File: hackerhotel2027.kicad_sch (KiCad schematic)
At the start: 22 parts, among them J1 USB device, J2 USB host, U1 CH32V208CBU6_C5713556, U2 TPD4E05U06DQAR, Y1 32.768KHz, Y2 tbd

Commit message: Fill out all component LCSC numbers and fix footprint associations
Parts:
- AE2: LCSC Part (none) -> -
- C1, C2: value 22p -> 9p; LCSC C1555 -> (none); LCSC Part (none) -> C1580
- C3, C4: LCSC Part (none) -> -; now not fitted; now left out of the parts list
- C32, C33, C34, C35: LCSC C307331 -> (none); LCSC Part (none) -> C307331
- C5, C6: LCSC Part (none) -> C327209
- C7: LCSC C5199872 -> (none); LCSC Part (none) -> C5199872
- J1: symbol mch2021-rescue:USB_C_Receptacle_USB2.0-Connector -> Connector:USB_C_Receptacle_USB2.0_16P; LCSC C165948 -> (none); LCSC Part (none) -> C165948
- J2: LCSC C42576 -> (none)
- L1: footprint (none) -> Inductor_SMD:L_01005_0402Metric; LCSC Part (none) -> C703123
- R1, R2: LCSC C25905 -> (none); LCSC Part (none) -> C25905
- R25: LCSC C60490 -> (none); LCSC Part (none) -> C60490
- U2: LCSC C138714 -> (none); LCSC Part (none) -> C138714
- Y1: LCSC C95361 -> (none); LCSC Part (none) -> C95361
- Y2: value tbd -> 32MHz; footprint (none) -> Crystal:Crystal_SMD_3225-4Pin_3.2x2.5mm; LCSC Part (none) -> C9009
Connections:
- net GND: now also J1.SH (SHIELD); no longer J1.S1 (SHIELD)
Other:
- sheet display ports: added BUSY, CS, DC, MOSI, RESETn, SCK; removed none
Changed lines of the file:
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@@
 	(generator_version "10.0")
 	(paper "A4")
+	(title_block
+		(date "2026-06-13")
+	)
 	(junction
 		(at 85.09 102.87)
@@
 			)
 		)
-		(property "LCSC" "C42576"
-			(at 163.83 27.94 0)
-			(hide yes)
-			(show_name no)
-			(do_not_autoplace no)
-			(effects
-				(font
-					(size 1.27 1.27)
-				)
-			)
-		)
 		(pin "5"
 		)
@@
 			)
 		)
-		(property "LCSC" "C138714"
-			(at 231.14 124.46 0)
+		(property "LCSC Part" "C138714"
+			(at 231.14 106.68 0)
 			(hide yes)
 			(show_name no)
@@
 			)
 		)
-		(property "LCSC" "C60490"
+		(property "LCSC Part" "C60490"
 			(at 100.33 78.74 0)
 			(hide yes)
@@
 			)
 		)
-		(property "LCSC" "C25905"
-			(at 245.11 85.09 0)
+		(property "LCSC Part" "C25905"
+			(at 245.11 85.09 90)
 			(hide yes)
 			(show_name no)
@@
 		(body_style 1)
 		(exclude_from_sim no)
-		(in_bom yes)
+		(in_bom no)
 		(on_board yes)
-		(in_pos_files yes)
-		(dnp no)
+		(in_pos_files no)
+		(dnp yes)
 		(property "Reference" "C3"
 			(at 90.678 106.934 0)
@@
 			)
 		)
-		(property "Datasheet" ""
+		(property "Datasheet" "-"
 			(at 90.17 109.22 0)
 			(hide yes)
@@
 			)
 		)
-		(property "LCSC" ""
+		(property "LCSC Part" "-"
 			(at 90.17 109.22 0)
 			(hide yes)
@@
 			)
 		)
-		(property "LCSC" "C5199872"
+		(property "LCSC Part" "C5199872"
 			(at 193.04 80.01 0)
 			(hide yes)
@@
 			)
 		)
-		(property "LCSC" "C307331"
+		(property "LCSC Part" "C307331"
 			(at 62.23 109.22 0)
 			(hide yes)
@@
 			)
 		)
-		(property "LCSC" "C307331"
+		(property "LCSC Part" "C307331"
 			(at 100.33 109.22 0)
 			(hide yes)
@@
 			)
 		)
-		(property "LCSC" "C307331"
+		(property "LCSC Part" "C307331"
 			(at 50.8 109.22 0)
 			(hide yes)
@@
 			)
 		)
-		(property "Datasheet" ""
+		(property "Datasheet" "https://www.lcsc.com/product-detail/C327209.html"
 			(at 193.04 62.23 0)
 			(hide yes)
@@
 			)
 		)
-		(property "LCSC" ""
+		(property "LCSC Part" "C327209"
 			(at 193.04 62.23 0)
 			(hide yes)
@@
 			)
 		)
-		(property "Value" "tbd"
+		(property "Value" "32MHz"
 			(at 88.646 102.616 90)
 			(show_name no)
@@
 			)
 		)
-		(property "Footprint" ""
+		(property "Footprint" "Crystal:Crystal_SMD_3225-4Pin_3.2x2.5mm"
 			(at 92.71 102.87 0)
 			(hide yes)
@@
 			)
 		)
-		(property "Datasheet" ""
+		(property "Datasheet" "https://www.lcsc.com/product-detail/C9009.html"
 			(at 92.71 102.87 0)
 			(hide yes)
@@
 			)
 		)
-		(property "LCSC" ""
+		(property "LCSC Part" "C9009"
 			(at 92.71 102.87 0)
 			(hide yes)
@@
 	)
 	(symbol
-		(lib_id "mch2021-rescue:USB_C_Receptacle_USB2.0-Connector")
+		(lib_id "Connector:USB_C_Receptacle_USB2.0_16P")
 		(at 265.43 92.71 0)
 		(mirror y)
@@
 			)
 		)
-		(property "Datasheet" "https://datasheet.lcsc.com/lcsc/2108131730_Korean-Hroparts-Elec-TYPE-C-31-M-12_C165948.pdf"
+		(property "Datasheet" "https://www.usb.org/sites/default/files/documents/usb_type-c.zip"
 			(at 261.62 92.71 0)
 			(hide yes)
@@
 			)
 		)
-		(property "Description" "TYPE-C-31-M-12"
+		(property "Description" "USB 2.0-only 16P Type-C Receptacle connector"
 			(at 265.43 92.71 0)
 			(hide yes)
@@
 			)
 		)
-		(property "LCSC" "C165948"
+		(property "FT Position Offset" "0,1"
 			(at 265.43 92.71 0)
 			(hide yes)
@@
 			)
 		)
-		(property "FT Position Offset" "0,1"
+		(property "LCSC Part" "C165948"
 			(at 265.43 92.71 0)
 			(hide yes)
@@
 		(pin "B9"
 		)
-		(pin "S1"
+		(pin "SH"
 		)
 		(instances
@@
 			)
 		)
-		(property "Datasheet" ""
+		(property "Datasheet" "-"
 			(at 213.36 48.26 0)
 			(hide yes)
@@
 			)
 		)
+		(property "LCSC Part" "-"
+			(at 213.36 48.26 0)
+			(hide yes)
+			(show_name no)
+			(do_not_autoplace no)
+			(effects
+				(font
+					(size 1.27 1.27)
+				)
+			)
+		)
 		(pin "1"
 		)
@@
 			)
 		)
-		(property "Value" "22p"
+		(property "Value" "9p"
 			(at 80.518 111.506 0)
 			(show_name no)
@@
 			)
 		)
-		(property "Datasheet" "https://datasheet.lcsc.com/lcsc/2304140030_FH--Guangdong-Fenghua-Advanced-Tech-0402CG220J500NT_C1555.pdf"
+		(property "Datasheet" "https://www.lcsc.com/product-detail/C1580.html"
 			(at 80.01 109.22 0)
 			(hide yes)
@@
 			)
 		)
-		(property "LCSC" "C1555"
+		(property "LCSC Part" "C1580"
 			(at 80.01 109.22 0)
 			(hide yes)
@@
 			)
 		)
-		(property "Value" "22p"
+		(property "Value" "9p"
 			(at 85.598 111.76 0)
 			(show_name no)
@@
 			)
 		)
-		(property "Datasheet" "https://datasheet.lcsc.com/lcsc/2304140030_FH--Guangdong-Fenghua-Advanced-Tech-0402CG220J500NT_C1555.pdf"
+		(property "Datasheet" "https://www.lcsc.com/product-detail/C1580.html"
 			(at 85.09 109.22 0)
 			(hide yes)
@@
 			)
 		)
-		(property "LCSC" "C1555"
+		(property "LCSC Part" "C1580"
 			(at 85.09 109.22 0)
 			(hide yes)
@@
 			)
 		)
-		(property "LCSC" "C307331"
+		(property "LCSC Part" "C307331"
 			(at 39.37 109.22 0)
 			(hide yes)
@@
 		(body_style 1)
 		(exclude_from_sim no)
-		(in_bom yes)
+		(in_bom no)
 		(on_board yes)
-		(in_pos_files yes)
-		(dnp no)
+		(in_pos_files no)
+		(dnp yes)
 		(property "Reference" "C4"
 			(at 95.758 106.934 0)
@@
 			)
 		)
-		(property "Datasheet" ""
+		(property "Datasheet" "-"
 			(at 95.25 109.22 0)
 			(hide yes)
@@
 			)
 		)
-		(property "LCSC" ""
+		(property "LCSC Part" "-"
 			(at 95.25 109.22 0)
 			(hide yes)
@@
 			)
 		)
-		(property "Datasheet" ""
+		(property "Datasheet" "https://www.lcsc.com/product-detail/C327209.html"
 			(at 205.74 62.23 0)
 			(hide yes)
@@
 			)
 		)
-		(property "LCSC" ""
+		(property "LCSC Part" "C327209"
 			(at 205.74 62.23 0)
 			(hide yes)
@@
 			)
 		)
-		(property "Footprint" ""
+		(property "Footprint" "Inductor_SMD:L_01005_0402Metric"
 			(at 199.39 55.88 0)
 			(hide yes)
@@
 			)
 		)
-		(property "Datasheet" ""
+		(property "Datasheet" "https://www.lcsc.com/product-detail/C703123.html?s_z=s_p_LQW15AN1N8C00D"
 			(at 199.39 55.88 0)
 			(hide yes)
@@
 			)
 		)
+		(property "LCSC Part" "C703123"
+			(at 199.39 55.88 90)
+			(hide yes)
+			(show_name no)
+			(do_not_autoplace no)
+			(effects
+				(font
+					(size 1.27 1.27)
+				)
+			)
+		)
 		(pin "2"
 		)
@@
 			)
 		)
-		(property "LCSC" "C25905"
-			(at 245.11 82.55 0)
+		(property "LCSC Part" "C25905"
+			(at 245.11 82.55 90)
 			(hide yes)
 			(show_name no)
@@
 			)
 		)
-		(property "LCSC" "C95361"
+		(property "LCSC Part" "C95361"
 			(at 82.55 102.87 0)
 			(hide yes)
@@
 	)
 	(sheet
-		(at 78.74 151.13)
-		(size 20.32 17.78)
+		(at 74.93 144.78)
+		(size 24.13 22.86)
 		(exclude_from_sim no)
 		(in_bom yes)
@@
 		)
 		(property "Sheetname" "display"
-			(at 78.74 150.4184 0)
+			(at 74.93 144.0684 0)
 			(show_name no)
 			(do_not_autoplace no)
@@
 		)
 		(property "Sheetfile" "display.kicad_sch"
-			(at 78.74 169.4946 0)
+			(at 74.93 168.2246 0)
 			(show_name no)
 			(do_not_autoplace no)
@@
 			)
 		)
+		(pin "BUSY" bidirectional
+			(at 74.93 149.86 180)
+			(effects
+				(font
+					(size 1.27 1.27)
+				)
+				(justify left)
+			)
+		)
+		(pin "CS" bidirectional
+			(at 74.93 152.4 180)
+			(effects
+				(font
+					(size 1.27 1.27)
+				)
+				(justify left)
+			)
+		)
+		(pin "DC" bidirectional
+			(at 74.93 154.94 180)
+			(effects
+				(font
+					(size 1.27 1.27)
+				)
+				(justify left)
+			)
+		)
+		(pin "MOSI" bidirectional
+			(at 90.17 144.78 90)
+			(effects
+				(font
+					(size 1.27 1.27)
+				)
+				(justify right)
+			)
+		)
+		(pin "RESETn" bidirectional
+			(at 74.93 160.02 180)
+			(effects
+				(font
+					(size 1.27 1.27)
+				)
+				(justify left)
+			)
+		)
+		(pin "SCK" bidirectional
+			(at 85.09 144.78 90)
+			(effects
+				(font
+					(size 1.27 1.27)
+				)
+				(justify right)
+			)
+		)

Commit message: Small tweaks & initial PCB work
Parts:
- added D1, D10, D11, D12, D13, D14, D15, D2, D4, D6, D7, D9: LED, symbol Device:LED
- added R3, R4, R5, R6: R, symbol Device:R
- added U3: TPD4E05U06DQAR, library:USON-10_L2.5-W1.0-P0.50-BL, symbol TPD4E05U06DQAR:TPD4E05U06DQAR_C138714
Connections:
- net GND: now also U3.3 (GND), U3.8 (GND)
- net SPI_MISO: now also U1.25 (PB14); no longer U1.15 (PA6/ADC6)
- net SPI_MOSI: now also U1.26 (PB15); no longer U1.16 (PA7/ADC7)
- net SPI_SCK: now also U1.24 (PB13); no longer U1.14 (PA5/ADC5)
- net VBUS: now also U3.4 (D2+), U3.5 (D2-), U3.6 (NC), U3.7 (NC)
- net at J2.2 (D-), U1.41 (PB6/USB2DM): now also U3.2 (D1-), U3.9 (NC)
- net at J2.3 (D+), U1.42 (PB7/USB2DP): now also U3.1 (D1+), U3.10 (NC)
- net T2: now reaches U1.11 (PA2/ADC2)
- net T3: now reaches U1.12 (PA3/ADC3)
- net T4: now reaches U1.13 (PA4/ADC4)
- net T8: now reaches U1.17 (PB0/ADC8)
- net T9: now reaches U1.18 (PB1/ADC9)
- net I2C2_SCL: now reaches U1.20 (PB10)
- net I2C2_SDA: now reaches U1.21 (PB11)
- net EPAPER_BUSY: now reaches U1.23 (PB12)
- net SPI_CS_EPAPER: now reaches U1.27 (PA8)
- net SPI_CS_FLASH: now reaches U1.28 (PA9)
- net EPAPER_DC: now reaches U1.29 (PA10)
- net LM4: now reaches U1.37 (PA15)
- net LM4: now also R6.1
- net LM3: now reaches U1.38 (PB3)
- net LM3: now also R5.1
- net LM2: now reaches U1.39 (PB4)
- net LM2: now also R4.1
- net LM1: now reaches U1.40 (PB5)
- net LM1: now also R3.1
- net BOOT: now reaches U1.43 (BOOT0)
- net I2C1_SCL: now reaches U1.44 (PB8)
- net I2C1_SDA: now reaches U1.45 (PB9)
- net BTN1 renamed PWR_BTN
- net BTN2 renamed T1
- new net: D12.1 (K), D13.2 (A), D14.1 (K), D15.2 (A), D7.1 (K), D9.2 (A), R6.2
- new net: D1.1 (K), D12.2 (A), D13.1 (K), D2.2 (A), D4.2 (A), D6.1 (K), R4.2
- new net: D6.2 (A), D7.2 (A)
- new net: D10.1 (K), D11.2 (A), D4.1 (K), D9.1 (K), R5.2
- new net: D1.2 (A), D10.2 (A), D11.1 (K), D14.2 (A), D15.1 (K), D2.1 (K), R3.2
- new net T5: U1.14 (PA5/ADC5)
- new net T6: U1.15 (PA6/ADC6)
- new net T7: U1.16 (PA7/ADC7)
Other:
- moved on the sheet: J2

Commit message: Switch to WCH ledmatrix controller, add loads of LEDs
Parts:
- removed AE2: Antenna, RF_Antenna:Texas_SWRA117D_2.4GHz_Right, symbol Device:Antenna_Loop
- removed C1, C2: 9p, Capacitor_SMD:C_0402_1005Metric, symbol Device:C
- removed C3, C4: (no value), Capacitor_SMD:C_0402_1005Metric, symbol Device:C
- removed C32: 100n, Capacitor_SMD:C_0402_1005Metric, symbol symbols:C
- removed C5, C6: 1.8p, Capacitor_SMD:C_0402_1005Metric, symbol Device:C
- removed C7: 1u, Capacitor_SMD:C_0603_1608Metric, symbol mch2021-rescue:C-Device
- removed J2: USB host, library:USB-A-TH_JTJ-USB-A-F-10.0-010, symbol Connector:USB_A
- removed L1: 1.8n, Inductor_SMD:L_01005_0402Metric, symbol Device:L
- removed R25: 10k, Resistor_SMD:R_0402_1005Metric, symbol symbols:R
- removed U1: CH32V208CBU6_C5713556, ch32v208:QFN-48_L5.0-W5.0-P0.35-BL-EP-A, symbol ch32v208:CH32V208CBU6_C5713556
- removed U3: TPD4E05U06DQAR, library:USON-10_L2.5-W1.0-P0.50-BL, symbol TPD4E05U06DQAR:TPD4E05U06DQAR_C138714
- removed Y1: 32.768KHz, Crystal:Crystal_SMD_3215-2Pin_3.2x1.5mm, symbol symbols:Crystal_Small
- removed Y2: 32MHz, Crystal:Crystal_SMD_3225-4Pin_3.2x2.5mm, symbol symbols:Crystal_Small
- added D100, D101, D102, D103, D104, D105, D106, D107, D108, D109, D110, D111, D112, D113, D114, D115, D116, D117, D118, D119, D120, D121, D122, D123, D124, D125, D126, D127, D128, D129, D130, D131, D132, D133, D134, D135, D136, D137, D138, D139, D140, D141, D142, D143, D144, D145, D146, D147, D148, D149, D150, D158, D159, D16, D160, D161, D162, D163, D164, D165, D166, D167, D168, D169, D17, D170, D171, D172, D173, D174, D175, D176, D177, D178, D179, D18, D180, D181, D182, D183, D184, D185, D186, D187, D188, D189, D19, D190, D191, D192, D193, D194, D195, D196, D197, D198, D199, D20, D200, D201, D202, D203, D204, D205, D206, D207, D208, D21, D216, D217, D218, D219, D22, D220, D221, D222, D223, D224, D225, D226, D227, D228, D229, D23, D230, D231, D232, D233, D234, D235, D236, D237, D238, D239, D24, D240, D241, D242, D243, D244, D245, D246, D247, D248, D249, D25, D250, D251, D252, D253, D254, D255, D256, D257, D258, D259, D26, D260, D261, D262, D263, D264, D265, D266, D27, D274, D275, D276, D277, D278, D279, D28, D280, D281, D282, D283, D284, D285, D286, D287, D288, D289, D29, D290, D291, D292, D293, D294, D295, D296, D297, D298, D299, D3, D30, D300, D301, D302, D303, D304, D305, D306, D307, D308, D309, D31, D310, D311, D312, D313, D314, D32, D33, D34, D42, D43, D44, D45, D46, D47, D48, D49, D5, D50, D51, D52, D53, D54, D55, D56, D57, D58, D59, D60, D61, D62, D63, D64, D65, D66, D67, D68, D69, D70, D71, D72, D73, D74, D75, D76, D77, D78, D79, D8, D80, D81, D82, D83, D84, D85, D86, D87, D88, D89, D90, D91, D92: LED, LED_SMD:LED_0402_1005Metric, symbol Device:LED
- added D151, D152, D153, D154, D155, D156, D157, D209, D210, D211, D212, D213, D214, D215, D267, D268, D269, D270, D271, D272, D273, D35, D36, D37, D38, D39, D40, D41, D93, D94, D95, D96, D97, D98, D99: NH-B1515RGBA-GF, led:LED-SMD-4P-L1.6-W1.5_NH-B1515RGBA-GF, symbol led:NH-B1515RGBA-GF
- added R1, R10, R11, R12, R13, R14, R15, R16, R17, R18, R19, R2, R20, R21, R22, R23, R24, R7, R8, R9: R, Resistor_SMD:R_0402_1005Metric, symbol Device:R
- added U1: CH643Q, ch643:LQFP-64_L7.0-W7.0-P0.40-LS9.2-BL, symbol ch643:CH643Q
- D1, D10, D11, D12, D13, D14, D15, D2, D4, D6, D7, D9: footprint (none) -> LED_SMD:LED_0402_1005Metric; LCSC Part (none) -> C779450
- R3, R4, R5, R6: footprint (none) -> Resistor_SMD:R_0402_1005Metric
- renumbered C35 to C1, C34 to C2, C33 to C3, R1 to R25, R2 to R26
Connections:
- net CC1: now also U1.55 (PC14/CC1/T1C3_/T2C2_)
- net CC2: now also U1.56 (PC15/CC2/T2C3_/T1ET_)
- net GND: now also U1.1 (GND), U1.30 (GND30)
- net T1: now also U1.9 (PC0/TX2_/T2C4_)
- net T2: now also U1.10 (PC1/T1C2_/T2C1N_)
- net T3: now also U1.11 (PC2/T1C3_/T2C2N_)
- net T4: now also U1.12 (PC3/RTS2_/T1C4_)
- net R6b: now reaches D6.2 (A)
- net R6b: now also R6.2, D105.2 (A), D122.2 (A), D139.2 (A), D163.2 (A), D180.2 (A), D197.2 (A), D221.2 (A), D23.2 (A), D238.2 (A), D255.2 (A), D279.2 (A), D296.2 (A), D47.2 (A), D64.2 (A), D81.2 (A); no longer D7.2 (A)
- net C1: now reaches D10.1 (K), D4.1 (K), D9.1 (K)
- net C1: now also D1.1 (K), D11.1 (K), D12.1 (K), D13.1 (K), D14.1 (K), D15.1 (K), D2.1 (K), D6.1 (K), D7.1 (K), D16.1 (K), D17.1 (K), D3.1 (K), D35.1 (RED), D36.1 (RED), D37.1 (RED), D38.1 (RED), D39.1 (RED), D40.1 (RED), D41.1 (RED), D5.1 (K), D8.1 (K), U1.25 (PB0/TX4/T1C2N_/O1P0); no longer D11.2 (A), R5.2
- net USB_DN: now reaches J1.A7 (D-), J1.B7 (D-), U2.1 (D1+), U2.10 (NC)
- net USB_DN: now also U1.43 (PC16/UDM/T1C4/TX4_)
- net USB_DP: now reaches J1.A6 (D+), J1.B6 (D+), U2.2 (D1-), U2.9 (NC)
- net USB_DP: now also U1.44 (PC17/UDP/RTS1/TX4_)
- net LM1 renamed R3
- net R3: now also U1.17 (PA2/TX2/T2C3/O2O1)
- net LM2 renamed R4
- net R4: now also U1.18 (PA3/T2C4/O1O0)
- net LM3 renamed R5
- net R5: now also U1.21 (PA4/CS/O2O0/RTS3_)
- net LM4 renamed R6
- net R6: now also U1.22 (PA5/SCK/TX4_/CTS4_)
- new net: D152.2, D210.2, D268.2, D309.2 (A), D36.2, D94.2, R19.2
- new net: D151.2, D209.2, D267.2, D308.2 (A), D35.2, D93.2, R18.2
- new net: D156.2, D214.2, D272.2, D313.2 (A), D40.2, D98.2, R23.2
- new net: D116.2 (A), D133.2 (A), D150.2 (A), D17.2 (A), D174.2 (A), D191.2 (A), D208.2 (A), D232.2 (A), D249.2 (A), D266.2 (A), D290.2 (A), D307.2 (A), D34.2 (A), D58.2 (A), D75.2 (A), D92.2 (A), R17.2
- new net: D114.2 (A), D131.2 (A), D148.2 (A), D15.2 (A), D172.2 (A), D189.2 (A), D206.2 (A), D230.2 (A), D247.2 (A), D264.2 (A), D288.2 (A), D305.2 (A), D32.2 (A), D56.2 (A), D73.2 (A), D90.2 (A), R15.2
- new net: D153.2, D211.2, D269.2, D310.2 (A), D37.2, D95.2, R20.2
- new net: D157.2, D215.2, D273.2, D314.2 (A), D41.2, D99.2, R24.2
- new net: D115.2 (A), D132.2 (A), D149.2 (A), D16.2 (A), D173.2 (A), D190.2 (A), D207.2 (A), D231.2 (A), D248.2 (A), D265.2 (A), D289.2 (A), D306.2 (A), D33.2 (A), D57.2 (A), D74.2 (A), D91.2 (A), R16.2
- new net: D154.2, D212.2, D270.2, D311.2 (A), D38.2, D96.2, R21.2
- new net: D155.2, D213.2, D271.2, D312.2 (A), D39.2, D97.2, R22.2
- new net C10: D175.1 (K), D176.1 (K), D177.1 (K), D178.1 (K), D179.1 (K), D180.1 (K), D181.1 (K), D182.1 (K), D183.1 (K), D184.1 (K), D185.1 (K), D186.1 (K), D187.1 (K), D188.1 (K), D189.1 (K), D190.1 (K), D191.1 (K), D209.1 (RED), D210.1 (RED), D211.1 (RED), D212.1 (RED), D213.1 (RED), D214.1 (RED), D215.1 (RED), U1.40 (PB9/T1C1/MCO/TX4_40)
- new net C11: D192.1 (K), D193.1 (K), D194.1 (K), D195.1 (K), D196.1 (K), D197.1 (K), D198.1 (K), D199.1 (K), D200.1 (K), D201.1 (K), D202.1 (K), D203.1 (K), D204.1 (K), D205.1 (K), D206.1 (K), D207.1 (K), D208.1 (K), D209.4 (GREEN), D210.4 (GREEN), D211.4 (GREEN), D212.4 (GREEN), D213.4 (GREEN), D214.4 (GREEN), D215.4 (GREEN), U1.41 (PB10/TX1/T1C241)
- new net C12: D209.3 (BLUE), D210.3 (BLUE), D211.3 (BLUE), D212.3 (BLUE), D213.3 (BLUE), D214.3 (BLUE), D215.3 (BLUE), D216.1 (K), D217.1 (K), D218.1 (K), D219.1 (K), D220.1 (K), D221.1 (K), D222.1 (K), D223.1 (K), D224.1 (K), D225.1 (K), D226.1 (K), D227.1 (K), D228.1 (K), D229.1 (K), D230.1 (K), D231.1 (K), D232.1 (K), U1.42 (PB11/T1C3/T2C1N_/RX142)
- new net C13: D233.1 (K), D234.1 (K), D235.1 (K), D236.1 (K), D237.1 (K), D238.1 (K), D239.1 (K), D240.1 (K), D241.1 (K), D242.1 (K), D243.1 (K), D244.1 (K), D245.1 (K), D246.1 (K), D247.1 (K), D248.1 (K), D249.1 (K), D267.1 (RED), D268.1 (RED), D269.1 (RED), D270.1 (RED), D271.1 (RED), D272.1 (RED), D273.1 (RED), U1.46 (PB12/T1C4_/T2C2N_46)
- new net C14: D250.1 (K), D251.1 (K), D252.1 (K), D253.1 (K), D254.1 (K), D255.1 (K), D256.1 (K), D257.1 (K), D258.1 (K), D259.1 (K), D260.1 (K), D261.1 (K), D262.1 (K), D263.1 (K), D264.1 (K), D265.1 (K), D266.1 (K), D267.4 (GREEN), D268.4 (GREEN), D269.4 (GREEN), D270.4 (GREEN), D271.4 (GREEN), D272.4 (GREEN), D273.4 (GREEN), U1.48 (PB13/TX4_48)
- new net C15: D267.3 (BLUE), D268.3 (BLUE), D269.3 (BLUE), D270.3 (BLUE), D271.3 (BLUE), D272.3 (BLUE), D273.3 (BLUE), D274.1 (K), D275.1 (K), D276.1 (K), D277.1 (K), D278.1 (K), D279.1 (K), D280.1 (K), D281.1 (K), D282.1 (K), D283.1 (K), D284.1 (K), D285.1 (K), D286.1 (K), D287.1 (K), D288.1 (K), D289.1 (K), D290.1 (K), U1.49 (PB14/RX3_)
- new net C16: D291.1 (K), D292.1 (K), D293.1 (K), D294.1 (K), D295.1 (K), D296.1 (K), D297.1 (K), D298.1 (K), D299.1 (K), D300.1 (K), D301.1 (K), D302.1 (K), D303.1 (K), D304.1 (K), D305.1 (K), D306.1 (K), D307.1 (K), D308.1 (K), D309.1 (K), D310.1 (K), D311.1 (K), D312.1 (K), D313.1 (K), D314.1 (K), U1.54 (PB15/T2C2_/SCK_/CTS4)
- new net C2: D18.1 (K), D19.1 (K), D20.1 (K), D21.1 (K), D22.1 (K), D23.1 (K), D24.1 (K), D25.1 (K), D26.1 (K), D27.1 (K), D28.1 (K), D29.1 (K), D30.1 (K), D31.1 (K), D32.1 (K), D33.1 (K), D34.1 (K), D35.4 (GREEN), D36.4 (GREEN), D37.4 (GREEN), D38.4 (GREEN), D39.4 (GREEN), D40.4 (GREEN), D41.4 (GREEN), U1.26 (PB1/T1C3N_/RX4)
- new net C3: D35.3 (BLUE), D36.3 (BLUE), D37.3 (BLUE), D38.3 (BLUE), D39.3 (BLUE), D40.3 (BLUE), D41.3 (BLUE), D42.1 (K), D43.1 (K), D44.1 (K), D45.1 (K), D46.1 (K), D47.1 (K), D48.1 (K), D49.1 (K), D50.1 (K), D51.1 (K), D52.1 (K), D53.1 (K), D54.1 (K), D55.1 (K), D56.1 (K), D57.1 (K), D58.1 (K), U1.27 (PB2/C2O/RX1_27)
- new net C4: D59.1 (K), D60.1 (K), D61.1 (K), D62.1 (K), D63.1 (K), D64.1 (K), D65.1 (K), D66.1 (K), D67.1 (K), D68.1 (K), D69.1 (K), D70.1 (K), D71.1 (K), D72.1 (K), D73.1 (K), D74.1 (K), D75.1 (K), D93.1 (RED), D94.1 (RED), D95.1 (RED), D96.1 (RED), D97.1 (RED), D98.1 (RED), D99.1 (RED), U1.28 (PB3/TX3/C3O/T2C3_)
- new net C5: D76.1 (K), D77.1 (K), D78.1 (K), D79.1 (K), D80.1 (K), D81.1 (K), D82.1 (K), D83.1 (K), D84.1 (K), D85.1 (K), D86.1 (K), D87.1 (K), D88.1 (K), D89.1 (K), D90.1 (K), D91.1 (K), D92.1 (K), D93.4 (GREEN), D94.4 (GREEN), D95.4 (GREEN), D96.4 (GREEN), D97.4 (GREEN), D98.4 (GREEN), D99.4 (GREEN), U1.29 (PB4/T2C4_/T3C1_/T2BK_)
- new net C6: D100.1 (K), D101.1 (K), D102.1 (K), D103.1 (K), D104.1 (K), D105.1 (K), D106.1 (K), D107.1 (K), D108.1 (K), D109.1 (K), D110.1 (K), D111.1 (K), D112.1 (K), D113.1 (K), D114.1 (K), D115.1 (K), D116.1 (K), D93.3 (BLUE), D94.3 (BLUE), D95.3 (BLUE), D96.3 (BLUE), D97.3 (BLUE), D98.3 (BLUE), D99.3 (BLUE), U1.32 (PB5/O1O1/T3C2_)
- new net C7: D117.1 (K), D118.1 (K), D119.1 (K), D120.1 (K), D121.1 (K), D122.1 (K), D123.1 (K), D124.1 (K), D125.1 (K), D126.1 (K), D127.1 (K), D128.1 (K), D129.1 (K), D130.1 (K), D131.1 (K), D132.1 (K), D133.1 (K), D151.1 (RED), D152.1 (RED), D153.1 (RED), D154.1 (RED), D155.1 (RED), D156.1 (RED), D157.1 (RED), U1.33 (PB6/T1C1N/CTS3/O1N133)
- new net C8: D134.1 (K), D135.1 (K), D136.1 (K), D137.1 (K), D138.1 (K), D139.1 (K), D140.1 (K), D141.1 (K), D142.1 (K), D143.1 (K), D144.1 (K), D145.1 (K), D146.1 (K), D147.1 (K), D148.1 (K), D149.1 (K), D150.1 (K), D151.4 (GREEN), D152.4 (GREEN), D153.4 (GREEN), D154.4 (GREEN), D155.4 (GREEN), D156.4 (GREEN), D157.4 (GREEN), U1.34 (PB7/T1C2N/RTS3_/O2P234)
- new net C9: D151.3 (BLUE), D152.3 (BLUE), D153.3 (BLUE), D154.3 (BLUE), D155.3 (BLUE), D156.3 (BLUE), D157.3 (BLUE), D158.1 (K), D159.1 (K), D160.1 (K), D161.1 (K), D162.1 (K), D163.1 (K), D164.1 (K), D165.1 (K), D166.1 (K), D167.1 (K), D168.1 (K), D169.1 (K), D170.1 (K), D171.1 (K), D172.1 (K), D173.1 (K), D174.1 (K), U1.35 (PB8/T1C3N/O1P135)
- new net R1: R1.1, U1.15 (PA0/T2C1/CTS2)
- new net R10: R10.1, U1.58 (PA9/MOSI_/MISO_/RX4_)
- new net R10b: D10.2 (A), D109.2 (A), D126.2 (A), D143.2 (A), D167.2 (A), D184.2 (A), D201.2 (A), D225.2 (A), D242.2 (A), D259.2 (A), D27.2 (A), D283.2 (A), D300.2 (A), D51.2 (A), D68.2 (A), D85.2 (A), R10.2
- new net R11: R11.1, U1.59 (PA10/SCL/TX1_/MOSI_)
- new net R11b: D11.2 (A), D110.2 (A), D127.2 (A), D144.2 (A), D168.2 (A), D185.2 (A), D202.2 (A), D226.2 (A), D243.2 (A), D260.2 (A), D28.2 (A), D284.2 (A), D301.2 (A), D52.2 (A), D69.2 (A), D86.2 (A), R11.2
- new net R12: R12.1, U1.60 (PA11/SDA/SCK_/RX1_)
- new net R12b: D111.2 (A), D12.2 (A), D128.2 (A), D145.2 (A), D169.2 (A), D186.2 (A), D203.2 (A), D227.2 (A), D244.2 (A), D261.2 (A), D285.2 (A), D29.2 (A), D302.2 (A), D53.2 (A), D70.2 (A), D87.2 (A), R12.2
- new net R13: R13.1, U1.61 (PA12/CS_/T2C2_/T2C1N_)
- new net R13b: D112.2 (A), D129.2 (A), D13.2 (A), D146.2 (A), D170.2 (A), D187.2 (A), D204.2 (A), D228.2 (A), D245.2 (A), D262.2 (A), D286.2 (A), D30.2 (A), D303.2 (A), D54.2 (A), D71.2 (A), D88.2 (A), R13.2
- new net R14: R14.1, U1.62 (PA13/SCL_/RTS4_)
- new net R14b: D113.2 (A), D130.2 (A), D14.2 (A), D147.2 (A), D171.2 (A), D188.2 (A), D205.2 (A), D229.2 (A), D246.2 (A), D263.2 (A), D287.2 (A), D304.2 (A), D31.2 (A), D55.2 (A), D72.2 (A), D89.2 (A), R14.2
- new net R15: R15.1, U1.63 (PA14/SDA_/RTS1_)
- new net R16: R16.1, U1.2 (PA15/TX2_)
- new net R17: R17.1, U1.3 (PA16/RX2_)
- new net R18: R18.1, U1.4 (PA17/CTS2_)
- new net R19: R19.1, U1.5 (PA18/TX3_/T2ET_)
- new net R1b: D1.2 (A), D100.2 (A), D117.2 (A), D134.2 (A), D158.2 (A), D175.2 (A), D18.2 (A), D192.2 (A), D216.2 (A), D233.2 (A), D250.2 (A), D274.2 (A), D291.2 (A), D42.2 (A), D59.2 (A), D76.2 (A), R1.2
- new net R2: R2.1, U1.16 (PA1/RTS2/T2C2)
- new net R20: R20.1, U1.6 (PA19/T2ET/RX2_)
- new net R21: R21.1, U1.7 (PA20/TX2_/T2BK)
- new net R22: R22.1, U1.8 (PA21/T2C1N/RTS2_)
- new net R23: R23.1, U1.13 (PA22/T2C2N/C2N0)
- new net R24: R24.1, U1.14 (PA23/T2C3N/C1N1)
- new net R2b: D101.2 (A), D118.2 (A), D135.2 (A), D159.2 (A), D176.2 (A), D19.2 (A), D193.2 (A), D2.2 (A), D217.2 (A), D234.2 (A), D251.2 (A), D275.2 (A), D292.2 (A), D43.2 (A), D60.2 (A), D77.2 (A), R2.2
- new net R3b: D102.2 (A), D119.2 (A), D136.2 (A), D160.2 (A), D177.2 (A), D194.2 (A), D20.2 (A), D218.2 (A), D235.2 (A), D252.2 (A), D276.2 (A), D293.2 (A), D3.2 (A), D44.2 (A), D61.2 (A), D78.2 (A), R3.2
- new net R4b: D103.2 (A), D120.2 (A), D137.2 (A), D161.2 (A), D178.2 (A), D195.2 (A), D21.2 (A), D219.2 (A), D236.2 (A), D253.2 (A), D277.2 (A), D294.2 (A), D4.2 (A), D45.2 (A), D62.2 (A), D79.2 (A), R4.2
- new net R5b: D104.2 (A), D121.2 (A), D138.2 (A), D162.2 (A), D179.2 (A), D196.2 (A), D22.2 (A), D220.2 (A), D237.2 (A), D254.2 (A), D278.2 (A), D295.2 (A), D46.2 (A), D5.2 (A), D63.2 (A), D80.2 (A), R5.2
- new net R7: R7.1, U1.23 (PA6/MISO/T3C1/RTS4_)
- new net R7b: D106.2 (A), D123.2 (A), D140.2 (A), D164.2 (A), D181.2 (A), D198.2 (A), D222.2 (A), D239.2 (A), D24.2 (A), D256.2 (A), D280.2 (A), D297.2 (A), D48.2 (A), D65.2 (A), D7.2 (A), D82.2 (A), R7.2
- new net R8: R8.1, U1.24 (PA7/MOSI/T3C2/T1C1N_)
- new net R8b: D107.2 (A), D124.2 (A), D141.2 (A), D165.2 (A), D182.2 (A), D199.2 (A), D223.2 (A), D240.2 (A), D25.2 (A), D257.2 (A), D281.2 (A), D298.2 (A), D49.2 (A), D66.2 (A), D8.2 (A), D83.2 (A), R8.2
- new net R9: R9.1, U1.57 (PA8/MISO_/RTS4/RTS1_)
- new net R9b: D108.2 (A), D125.2 (A), D142.2 (A), D166.2 (A), D183.2 (A), D200.2 (A), D224.2 (A), D241.2 (A), D258.2 (A), D26.2 (A), D282.2 (A), D299.2 (A), D50.2 (A), D67.2 (A), D84.2 (A), D9.2 (A), R9.2
- new net SWCK: U1.47 (PC19/DCK/T2C1_)
- new net SWIO: U1.45 (PC18/DIO/TX3_/T2C1N_)
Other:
- removed sheet display
- moved on the sheet: C1, C2, C3, J1, R25, R26, U2

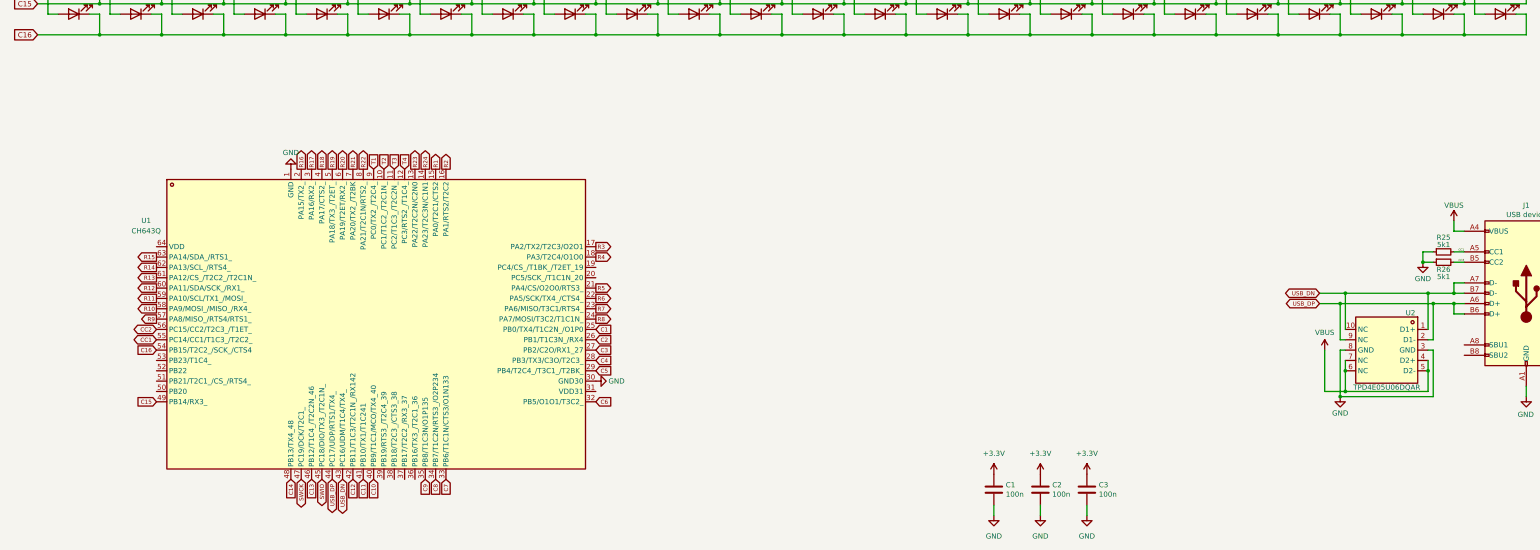
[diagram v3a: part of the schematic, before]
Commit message: Add battery circuit, more routing
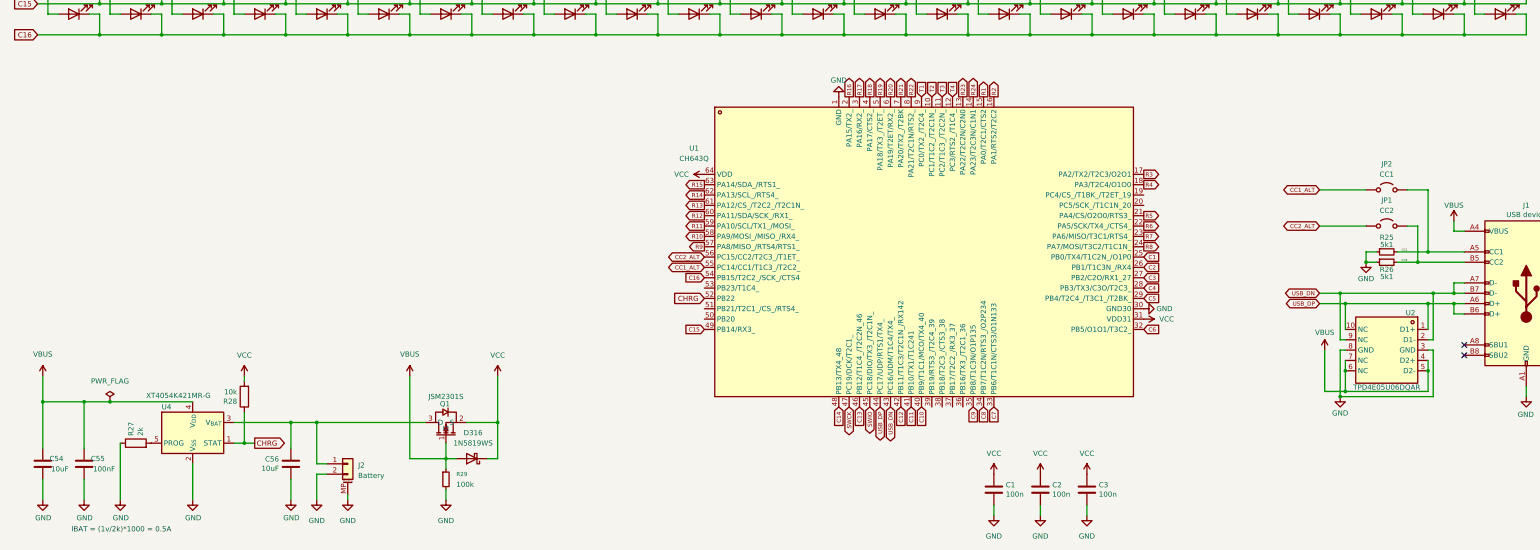
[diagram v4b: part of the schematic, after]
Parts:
- added C54, C56: 10uF, Capacitor_SMD:C_0603_1608Metric, symbol symbols:C
- added C55: 100nF, Capacitor_SMD:C_0402_1005Metric, symbol symbols:C
- added D316: 1N5819WS, Diode_SMD:D_SOD-323, symbol Diode:1N5819WS
- added J2: Battery, Connector_JST:JST_PH_B2B-PH-SM4-TB_1x02-1MP_P2.00mm_Vertical, symbol Connector_Generic_MountingPin:Conn_01x02_MountingPin
- added JP1: CC2, Jumper:SolderJumper-2_P1.3mm_Open_RoundedPad1.0x1.5mm, symbol Jumper:Jumper_2_Open
- added JP2: CC1, Jumper:SolderJumper-2_P1.3mm_Open_RoundedPad1.0x1.5mm, symbol Jumper:Jumper_2_Open
- added Q1: JSM2301S, Package_TO_SOT_SMD:SOT-23, symbol lcsc:JSM2301S
- added R27: 2k, Resistor_SMD:R_0402_1005Metric, symbol symbols:R
- added R28: 10k, Resistor_SMD:R_0402_1005Metric, symbol symbols:R
- added R29: 100k, Resistor_SMD:R_0402_1005Metric, symbol Device:R_Small
- added U4: XT4054K421MR-G, Package_TO_SOT_SMD:SOT-23-5, symbol Battery_Management:MCP73831-2-OT
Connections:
- net +3.3V is gone; now on net VCC: C1.1, C2.1, C3.1
- net CC1: now also JP2.2 (B); no longer U1.55 (PC14/CC1/T1C3_/T2C2_)
- net CC2: now also JP1.2 (B); no longer U1.56 (PC15/CC2/T2C3_/T1ET_)
- net GND: now also C54.1, C55.1, C56.2, J2.2 (Pin_2), J2.MP (MountPin), R27.1, R29.2, U4.2 (V_{SS})
- net USB_DN: now also U2.2 (D1-), U2.9 (NC); no longer U2.1 (D1+), U2.10 (NC)
- net USB_DP: now also U2.1 (D1+), U2.10 (NC); no longer U2.2 (D1-), U2.9 (NC)
- net VBUS: now also C54.2, C55.2, D316.2 (A), Q1.1 (G), R29.1, U4.4 (V_{DD})
- net VCC: now reaches U1.31 (VDD31)
- net VCC: now also U1.64 (VDD), D316.1 (K), Q1.2 (S), R28.2
- net CHRG: now reaches U1.52 (PB22)
- net CHRG: now also R28.1, U4.1 (STAT)
- new net: C56.1, J2.1 (Pin_1), Q1.3 (D), U4.3 (V_{BAT})
- new net: R27.2, U4.5 (PROG)
- new net CC1_ALT: JP2.1 (A), U1.55 (PC14/CC1/T1C3_/T2C2_)
- new net CC2_ALT: JP1.1 (A), U1.56 (PC15/CC2/T2C3_/T1ET_)
- no-connect marks 0 -> 2
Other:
- note added: "IBAT = (1v/2k)*1000 = 0.5A"
- moved on the sheet: R25, R26, U1
